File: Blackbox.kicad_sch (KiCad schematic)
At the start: 3 parts, among them U8 W25Q128JVPIQ

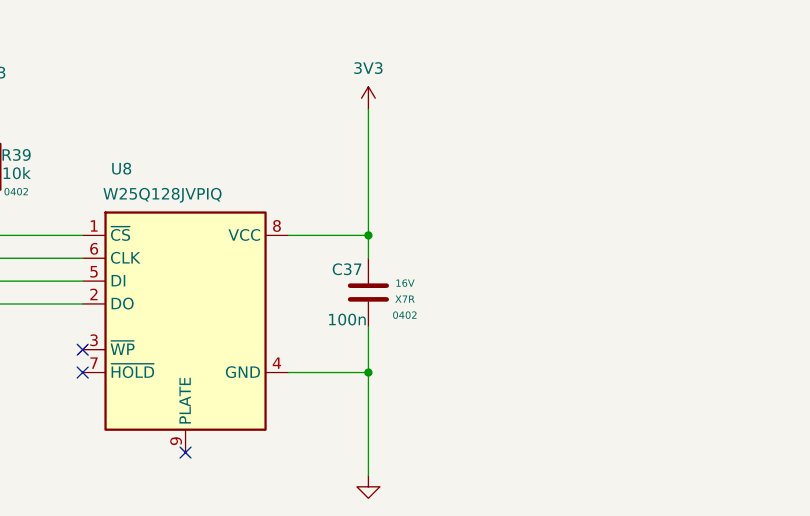
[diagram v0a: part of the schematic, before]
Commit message: Crystal change, gnd cut-out for crystal, bom update
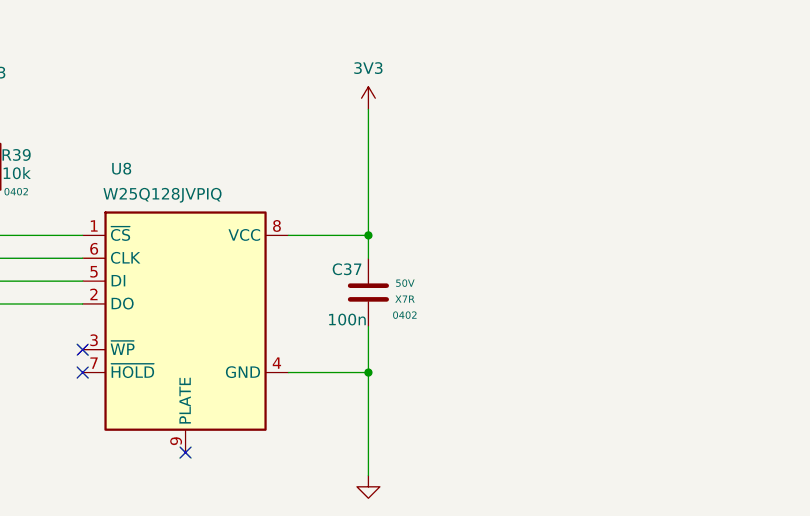
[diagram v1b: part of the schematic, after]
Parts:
- C37: JLCPCB # C71629 -> C77020; MANUFACTURER # GRM155R71C104KA88D -> GRM155R71H104KE14D; Unit Price 0.0016 -> (none); Voltage 16V -> 50V
- R39: Unit Price 0.0006 -> (none)
- U8: Unit Price 1.2495 -> (none)
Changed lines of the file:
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@@
 			)
 		)
-		(property "Datasheet" "https://jlcpcb.com/api/file/downloadByFileSystemAccessId/8588918717191229440"
+		(property "Datasheet" "https://www.lcsc.com/datasheet/C60490.pdf"
 			(at 87.63 49.53 0)
 			(effects
@@
 			)
 		)
-		(property "Ifrwd" ""
-			(at 87.63 49.53 0)
-			(effects
-				(font
-					(size 1.27 1.27)
-				)
-				(hide yes)
-			)
-		)
 		(property "MOUSER #" ""
-			(at 87.63 49.53 0)
-			(effects
-				(font
-					(size 1.27 1.27)
-				)
-				(hide yes)
-			)
-		)
-		(property "Freq" ""
-			(at 87.63 49.53 0)
-			(effects
-				(font
-					(size 1.27 1.27)
-				)
-				(hide yes)
-			)
-		)
-		(property "Unit Price" "0.0006"
 			(at 87.63 49.53 0)
 			(effects
@@
 			)
 		)
-		(property "Ifrwd" ""
-			(at 109.22 64.77 0)
-			(effects
-				(font
-					(size 1.27 1.27)
-				)
-				(hide yes)
-			)
-		)
 		(property "MOUSER #" ""
-			(at 109.22 64.77 0)
-			(effects
-				(font
-					(size 1.27 1.27)
-				)
-				(hide yes)
-			)
-		)
-		(property "Freq" ""
-			(at 109.22 64.77 0)
-			(effects
-				(font
-					(size 1.27 1.27)
-				)
-				(hide yes)
-			)
-		)
-		(property "Unit Price" "1.2495"
 			(at 109.22 64.77 0)
 			(effects
@@
 			)
 		)
-		(property "Datasheet" "https://pim.murata.com/asset/pim4/ceramicCapacitorSMD/GRM155R71C104KA88-01A-EN_PDF_CERAMICCAPACITORSMD?lastModifiedDatetime=20250813144737"
+		(property "Datasheet" "https://www.lcsc.com/datasheet/C77020.pdf"
 			(at 129.54 63.5 0)
 			(effects
@@
 			)
 		)
-		(property "Voltage" "16V"
+		(property "Voltage" "50V"
 			(at 133.604 62.484 0)
 			(effects
@@
 			)
 		)
-		(property "JLCPCB #" "C71629"
+		(property "JLCPCB #" "C77020"
 			(at 129.54 63.5 0)
 			(effects
@@
 			)
 		)
-		(property "MANUFACTURER #" "GRM155R71C104KA88D"
+		(property "MANUFACTURER #" "GRM155R71H104KE14D"
 			(at 129.54 63.5 0)
 			(effects
@@
 			)
 		)
-		(property "Ifrwd" ""
-			(at 129.54 63.5 0)
-			(effects
-				(font
-					(size 1.27 1.27)
-				)
-				(hide yes)
-			)
-		)
 		(property "MOUSER #" ""
 			(at 129.54 63.5 0)
 			(effects
-				(font
-					(size 1.27 1.27)
-				)
-				(hide yes)
-			)
-		)
-		(property "Freq" ""
-			(at 129.54 63.5 0)
-			(effects
-				(font
-					(size 1.27 1.27)
-				)
-				(hide yes)
-			)
-		)
-		(property "Unit Price" "0.0016"
-			(at 129.54 63.5 0)
-			(effects

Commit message: Updated
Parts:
- C37: JLCPCB # C77020 -> (none); LCSC (none) -> C77020
- R39: JLCPCB # C60490 -> (none); LCSC (none) -> C60490
- U8: JLCPCB # C190862 -> (none); LCSC (none) -> C190862
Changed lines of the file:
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@@
-			)
-		)
-		(property "JLCPCB #" "C60490"
-			(at 87.63 49.53 0)
-			(effects
-				(font
-					(size 1.27 1.27)
-				)
-				(hide yes)
 			)
 		)
@@
 		)
 		(property "Manufacturer #" ""
+			(at 87.63 49.53 0)
+			(effects
+				(font
+					(size 1.27 1.27)
+				)
+				(hide yes)
+			)
+		)
+		(property "LCSC" "C60490"
 			(at 87.63 49.53 0)
 			(effects
@@
 			)
 		)
-		(property "JLCPCB #" "C190862"
-			(at 109.22 64.77 0)
-			(effects
-				(font
-					(size 1.27 1.27)
-				)
-				(hide yes)
-			)
-		)
 		(property "Package" ""
 			(at 109.22 64.77 0)
@@
 		)
 		(property "Manufacturer #" ""
+			(at 109.22 64.77 0)
+			(effects
+				(font
+					(size 1.27 1.27)
+				)
+				(hide yes)
+			)
+		)
+		(property "LCSC" "C190862"
 			(at 109.22 64.77 0)
 			(effects
@@
 			)
 		)
-		(property "JLCPCB #" "C77020"
-			(at 129.54 63.5 0)
-			(effects
-				(font
-					(size 1.27 1.27)
-				)
-				(hide yes)
-			)
-		)
 		(property "MANUFACTURER" "Murata"
 			(at 129.54 63.5 0)
@@
 			(at 129.54 63.5 0)
 			(effects
+				(font
+					(size 1.27 1.27)
+				)
+				(hide yes)
+			)
+		)
+		(property "LCSC" "C77020"
+			(at 129.54 63.5 0)
+			(effects
